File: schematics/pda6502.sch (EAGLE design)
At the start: 6 parts, among them U1 W65C02S, U2 W65C22S, U3 KM28C64A-25, U4 UM61256AK-12

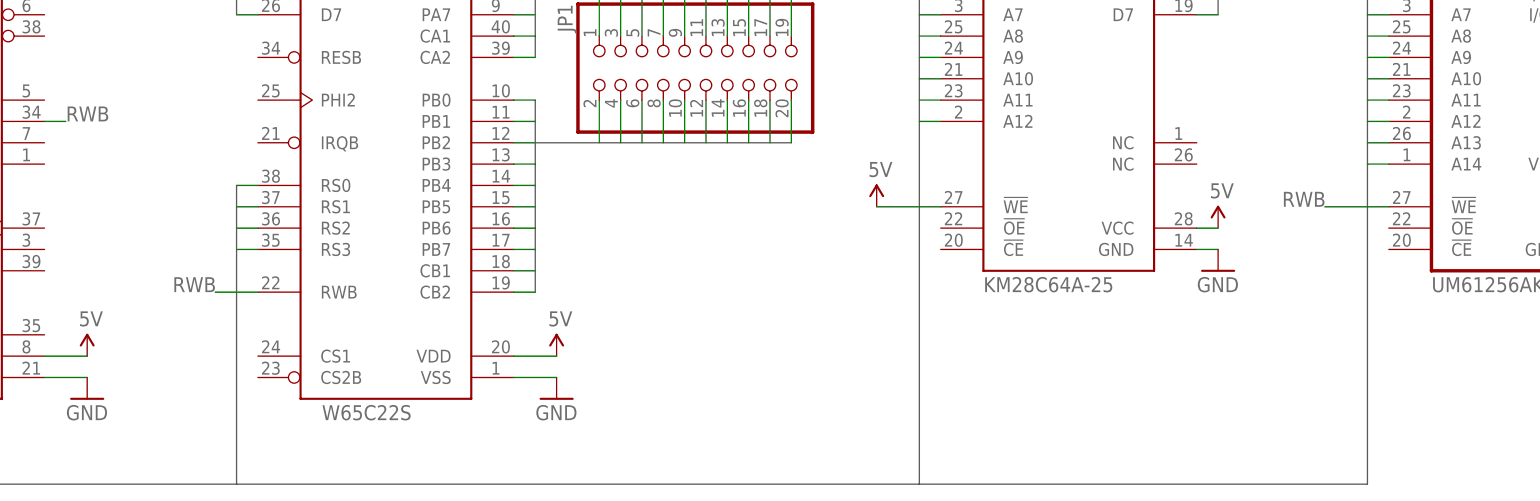
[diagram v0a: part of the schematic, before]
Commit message: schematics: OE and CE tied together, for ROM and RAM.
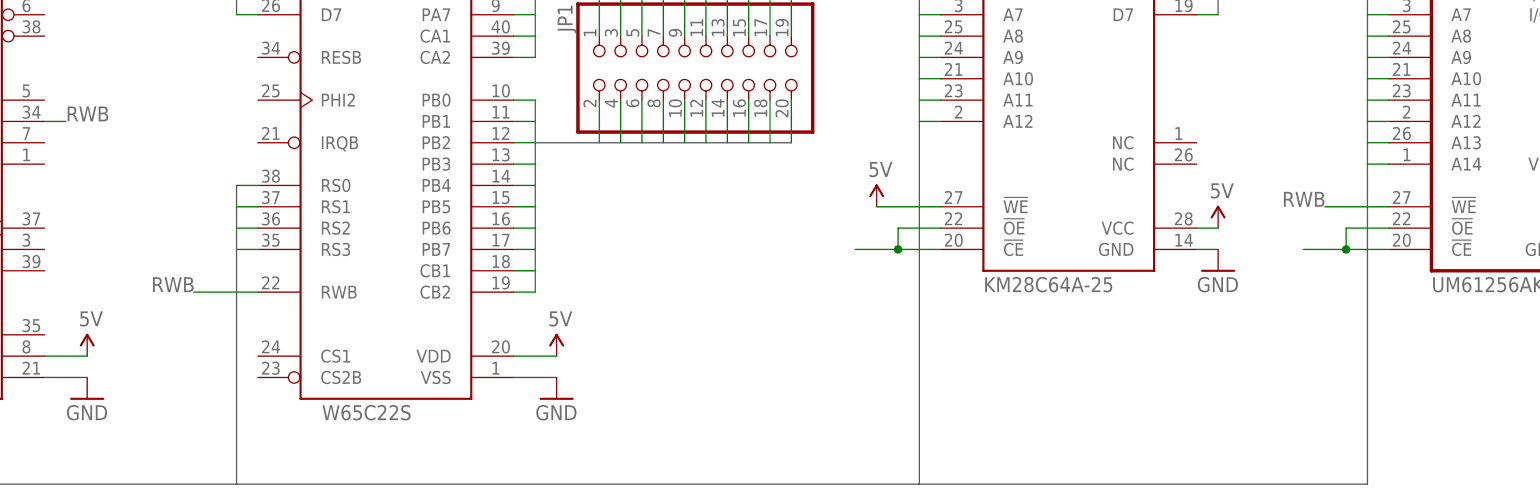
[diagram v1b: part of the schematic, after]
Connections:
- new net N$2: U3.!CE, U3.!OE
- new net N$3: U4.!CE, U4.!OE
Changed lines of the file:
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@@
 <segment>
 <pinref part="U2" gate="G$1" pin="RWB"/>
-<wire x1="101.6" y1="104.14" x2="96.52" y2="104.14" width="0.1524" layer="91"/>
-<label x="91.44" y="104.14" size="1.778" layer="95"/>
+<wire x1="101.6" y1="104.14" x2="93.98" y2="104.14" width="0.1524" layer="91"/>
+<label x="88.9" y="104.14" size="1.778" layer="95"/>
 </segment>
 <segment>
@@
 </segment>
 </net>
+<net name="N$2" class="0">
+<segment>
+<pinref part="U3" gate="G$1" pin="!CE"/>
+<wire x1="182.88" y1="109.22" x2="177.8" y2="109.22" width="0.1524" layer="91"/>
+<pinref part="U3" gate="G$1" pin="!OE"/>
+<wire x1="177.8" y1="109.22" x2="172.72" y2="109.22" width="0.1524" layer="91"/>
+<wire x1="182.88" y1="111.76" x2="177.8" y2="111.76" width="0.1524" layer="91"/>
+<wire x1="177.8" y1="111.76" x2="177.8" y2="109.22" width="0.1524" layer="91"/>
+<junction x="177.8" y="109.22"/>
+</segment>
+</net>
+<net name="N$3" class="0">
+<segment>
+<pinref part="U4" gate="G$1" pin="!CE"/>
+<wire x1="236.22" y1="109.22" x2="231.14" y2="109.22" width="0.1524" layer="91"/>
+<pinref part="U4" gate="G$1" pin="!OE"/>
+<wire x1="231.14" y1="109.22" x2="226.06" y2="109.22" width="0.1524" layer="91"/>
+<wire x1="236.22" y1="111.76" x2="231.14" y2="111.76" width="0.1524" layer="91"/>
+<wire x1="231.14" y1="111.76" x2="231.14" y2="109.22" width="0.1524" layer="91"/>
+<junction x="231.14" y="109.22"/>
+</segment>
+</net>

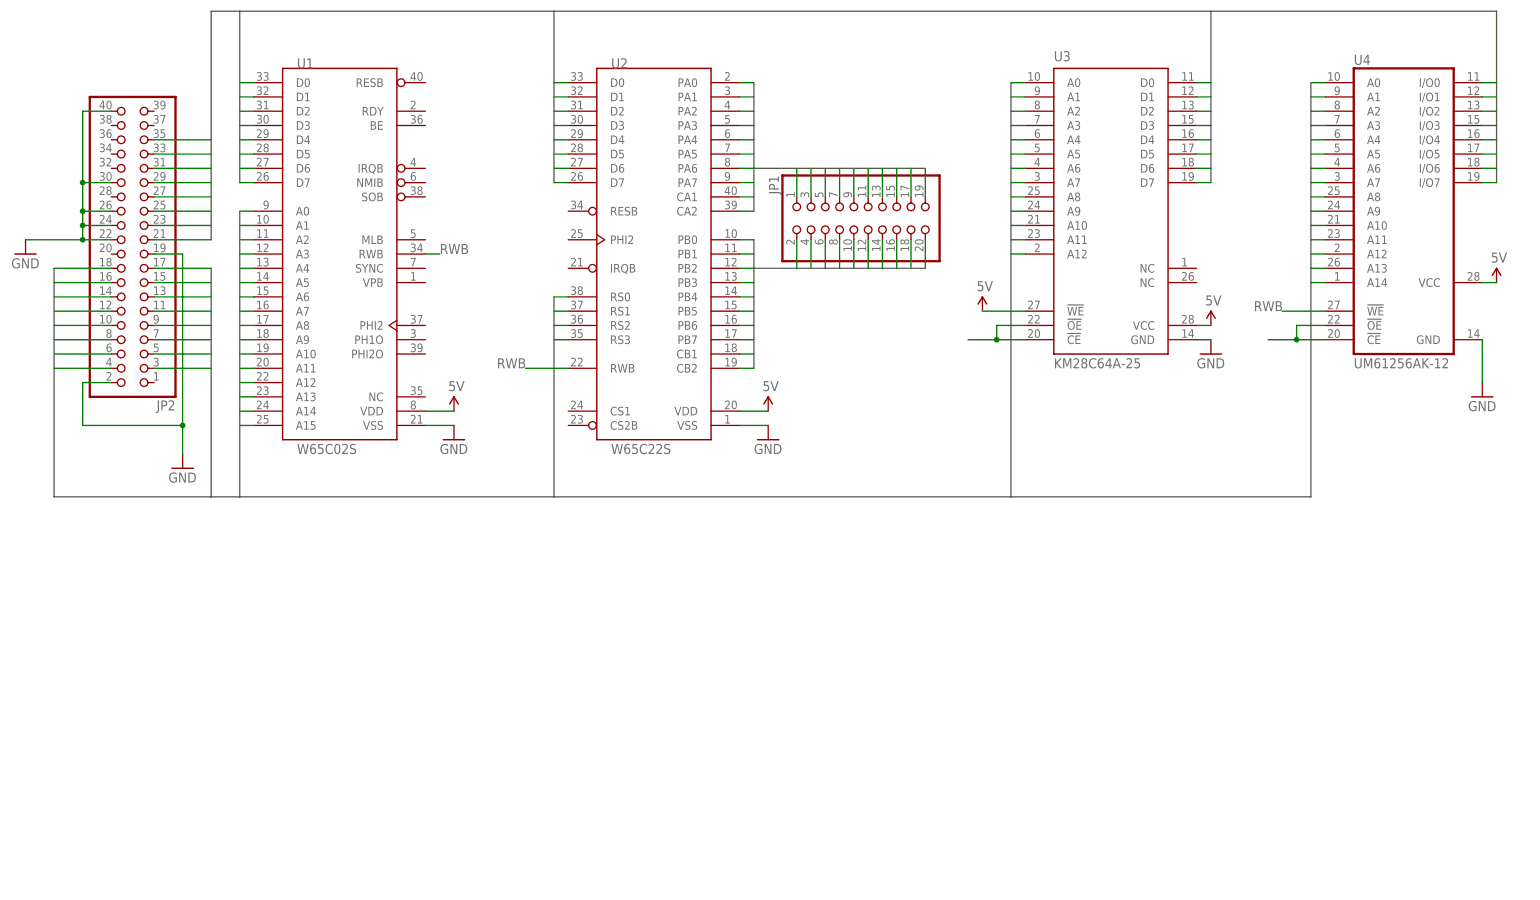
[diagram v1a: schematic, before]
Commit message: schematics: decoupling caps for all ICs; 0.1uF 0805 SMD.
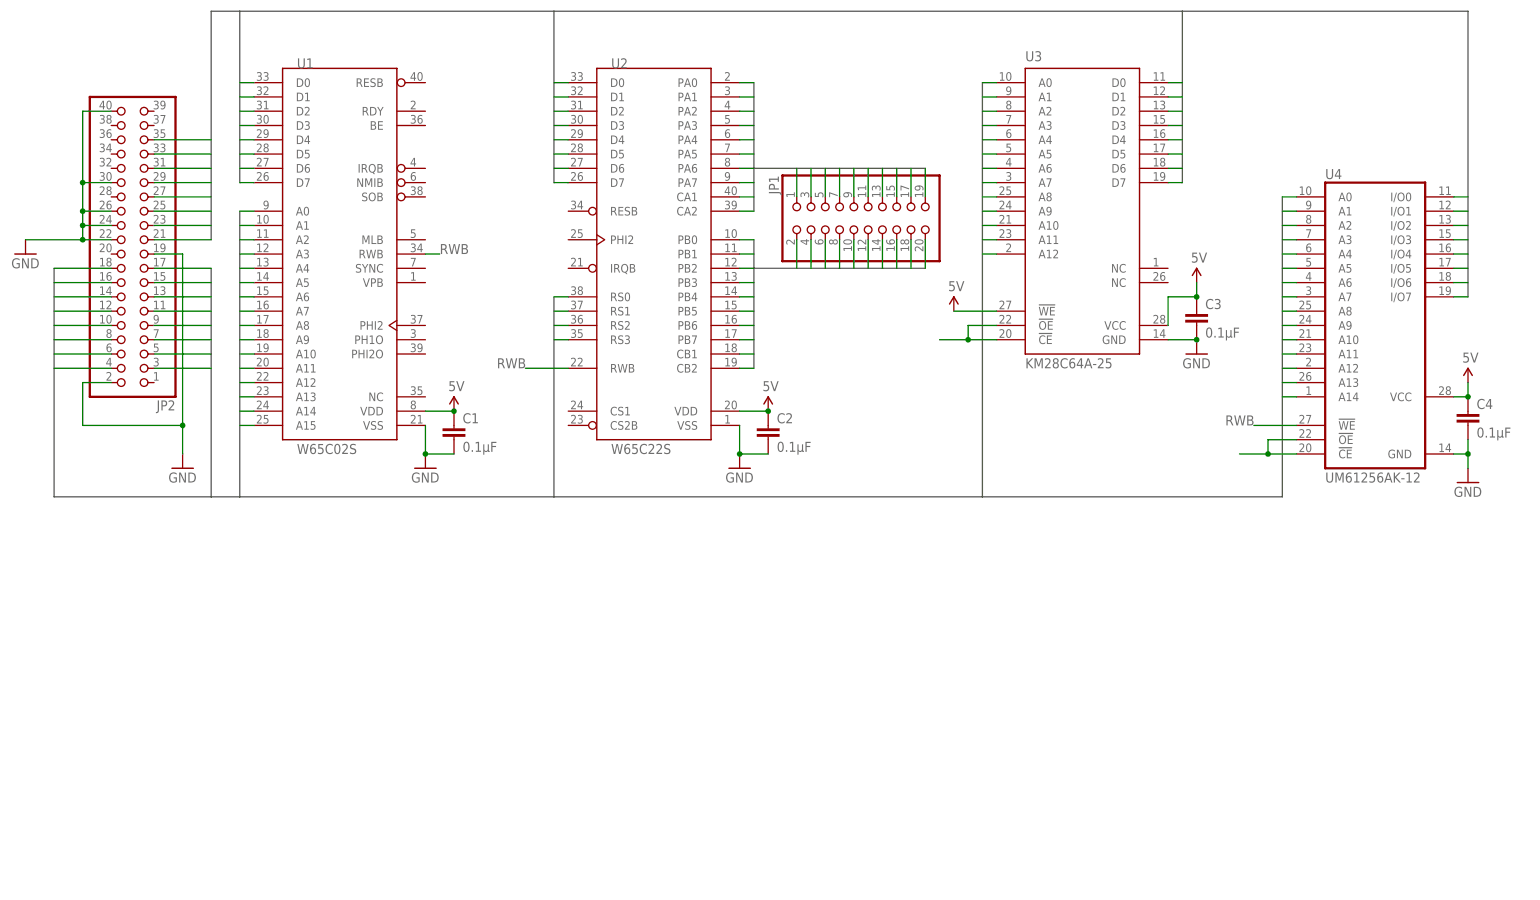
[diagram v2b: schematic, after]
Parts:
- added C1, C2, C3, C4: 0.1μF, rcl:C-EUC0805
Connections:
- net 5V: now also C1.1, C2.1, C3.1, C4.1
- net GND: now also C1.2, C2.2, C3.2, C4.2
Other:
- moved on the sheet: U3, U4

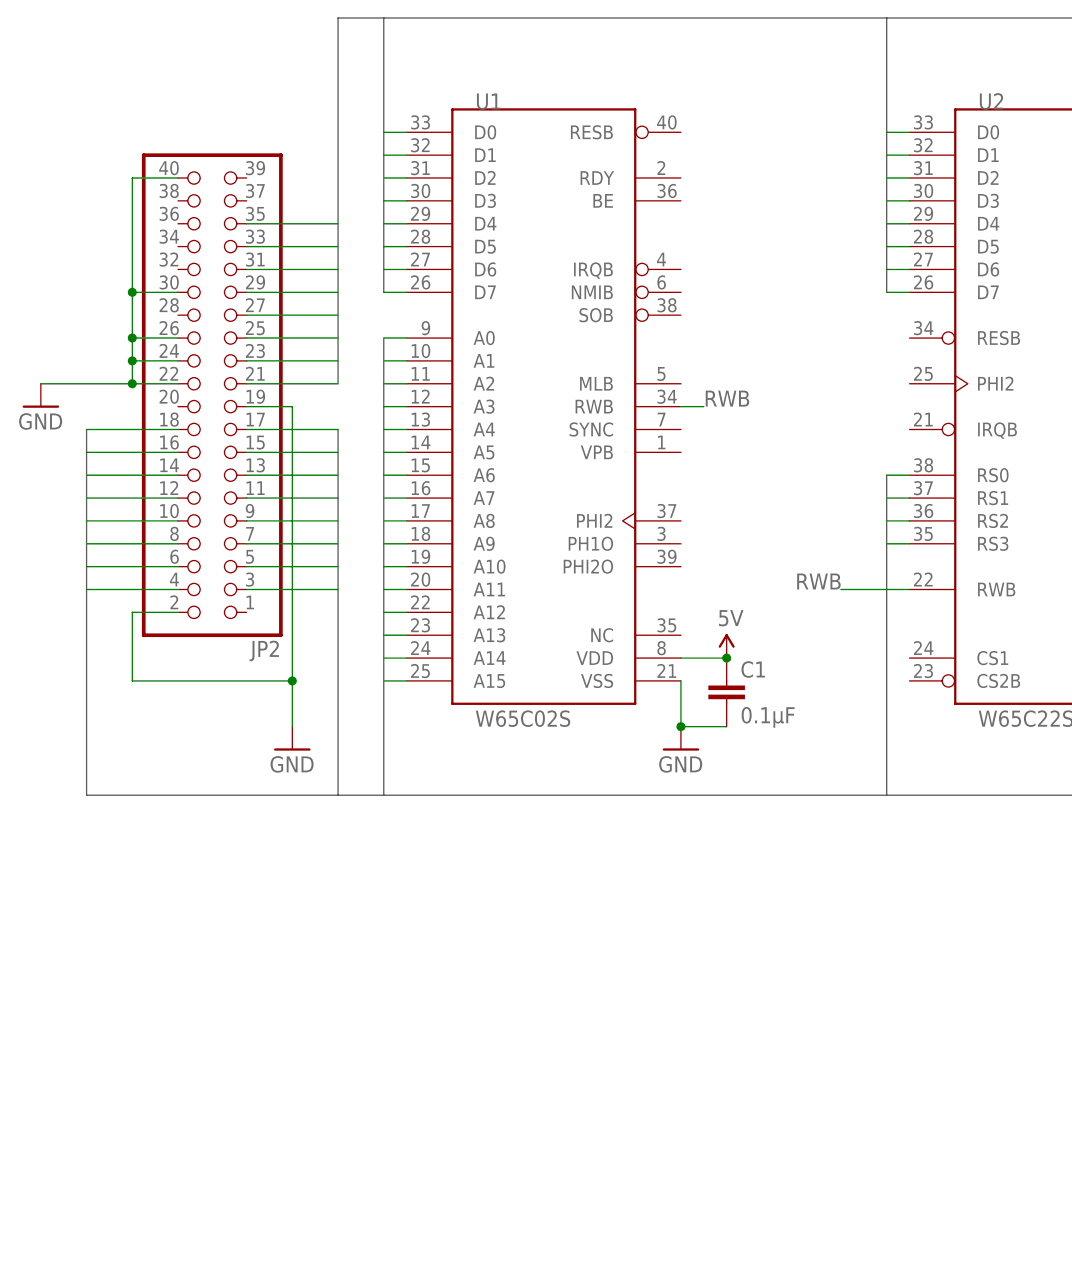
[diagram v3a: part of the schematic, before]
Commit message: schematics: reset circuit (DS1813); no button yet.
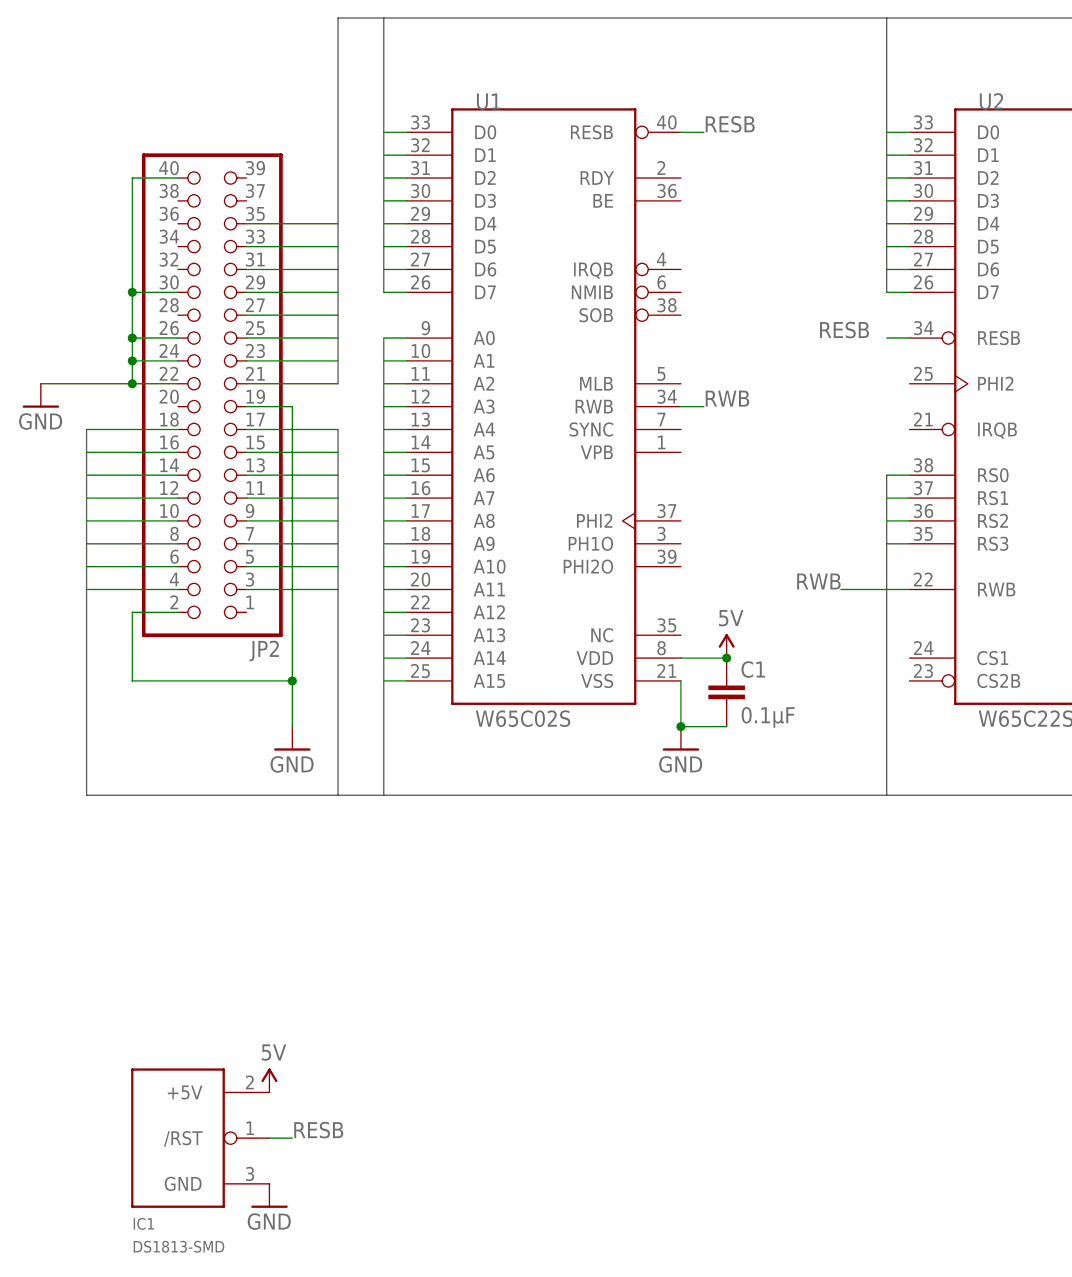
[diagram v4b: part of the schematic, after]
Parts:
- added IC1: DS1813-SMD, ds1813:DS1813-SMD
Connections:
- new net RESB: IC1./RST, U1.RESB, U2.RESB
- net 5V: now also IC1.+5V
- net GND: now also IC1.GND
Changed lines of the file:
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@@
 <part name="C3" library="rcl" deviceset="C-EU" device="C0805" value="0.1μF"/>
 <part name="C4" library="rcl" deviceset="C-EU" device="C0805" value="0.1μF"/>
+<part name="IC1" library="ds1813" deviceset="DS1813" device="-SMD"/>
+<part name="SUPPLY6" library="SparkFun-Aesthetics" deviceset="5V" device=""/>
+<part name="GND5" library="SparkFun-Aesthetics" deviceset="GND" device=""/>
 </parts>
 <sheets>
@@
 <instance part="C3" gate="G$1" x="213.36" y="114.3"/>
 <instance part="C4" gate="G$1" x="261.62" y="96.52"/>
+<instance part="IC1" gate="G$1" x="17.78" y="43.18"/>
+<instance part="SUPPLY6" gate="G$1" x="30.48" y="48.26"/>
+<instance part="GND5" gate="1" x="30.48" y="35.56"/>
 </instances>
 <busses>
@@
 <junction x="213.36" y="109.22"/>
 </segment>
+<segment>
+<pinref part="IC1" gate="G$1" pin="GND"/>
+<pinref part="GND5" gate="1" pin="GND"/>
+</segment>
 </net>
 <net name="5V" class="0">
@@
 <pinref part="C4" gate="G$1" pin="1"/>
 </segment>
+<segment>
+<pinref part="IC1" gate="G$1" pin="+5V"/>
+<pinref part="SUPPLY6" gate="G$1" pin="5V"/>
+</segment>
 </net>
 <net name="PA0" class="0">
@@
 </segment>
 </net>
+<net name="RESB" class="0">
+<segment>
+<pinref part="IC1" gate="G$1" pin="/RST"/>
+<wire x1="30.48" y1="43.18" x2="33.02" y2="43.18" width="0.1524" layer="91"/>
+<label x="33.02" y="43.18" size="1.778" layer="95"/>
+</segment>
+<segment>
+<pinref part="U1" gate="G$1" pin="RESB"/>
+<wire x1="76.2" y1="154.94" x2="78.74" y2="154.94" width="0.1524" layer="91"/>
+<label x="78.74" y="154.94" size="1.778" layer="95"/>
+</segment>
+<segment>
+<pinref part="U2" gate="G$1" pin="RESB"/>
+<wire x1="101.6" y1="132.08" x2="99.06" y2="132.08" width="0.1524" layer="91"/>
+<label x="91.44" y="132.08" size="1.778" layer="95"/>
+</segment>
+</net>
